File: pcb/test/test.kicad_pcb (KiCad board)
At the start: 2 copper layers, 12 parts, among them IC1 ADG904BRUZ-REEL7, J1 CONSMA013.062-G, J3 Conn_01x04, U1 MCP601R

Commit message: composants placés sur pcb
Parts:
- removed U1: MCP601R, Package_TO_SOT_SMD:SOT-23-5
- added ANT4: ST0147-00-011-A, test_footprint_library:ANTC3016X55N, F.Cu at (207.5, 20.0)
- added U2: TL081, Package_DIP:DIP-8_W7.62mm, F.Cu at (224.2, 135.7)
- moved C3 216.3 mm to (253.7, 131.5)
- moved R2 183.3 mm to (228.3, 114.0)
- moved R1 154.1 mm to (198.9, 111.0)
- moved C1 136.8 mm to (165.7, 150.5)
- moved C2 119.1 mm to (150.2, 149.5)
- moved ANT3 116.3 mm to (20.0, 20.0)
- moved ANT2 92.8 mm to (145.0, 20.0)
- moved ANT1 79.2 mm to (82.5, 20.0)
- moved J1 31.5 mm to (104.0, 168.6)
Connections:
- IC1 pad 14: unconnected-(IC1-RF4-Pad14) -> Net-(ANT4-FEED)

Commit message: pistes
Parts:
- added JP1: Jumper_2_Bridged, test_footprint_library:jumper20, F.Cu at (115.5, 96.5)
- added JP2: Jumper_2_Bridged, test_footprint_library:jumper20, F.Cu at (119.0, 91.0)
- moved C3 55.7 mm to (200.5, 115.0), turned to 90 degrees
- moved R2 41.8 mm to (187.5, 123.1), turned to 90 degrees
- moved R1 34.9 mm to (187.4, 144.0), turned to 90 degrees
- moved U2 21.2 mm to (205.4, 126.0), turned to -90 degrees
- moved C2 12.3 mm to (161.7, 145.0), turned to 180 degrees
- moved C1 5.80 mm to (161.5, 154.5), turned to 180 degrees
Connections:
- J3 pad 1: GND -> +5V
- J3 pad 2: Net-(IC1-A0) -> GND
- J3 pad 3: Net-(IC1-A1) -> Net-(J3-Pin_3)
- J3 pad 4: +5V -> Net-(J3-Pin_4)
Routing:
- net Net-(ANT4-FEED): track 0.00 -> 130.8 mm
- net +2V5: track 0.00 -> 129.6 mm
- net Net-(ANT3-FEED): track 0.00 -> 119.0 mm
- net GND: track 0.00 -> 99.2 mm
- net Net-(ANT2-FEED): track 0.00 -> 95.3 mm
- net Net-(ANT1-FEED): track 0.00 -> 88.7 mm
- net Net-(J3-Pin_4): track 0.00 -> 73.7 mm
- net Net-(J3-Pin_3): track 0.00 -> 69.8 mm
- net +5V: track 0.00 -> 67.9 mm
- net Net-(IC1-RFC): track 0.00 -> 63.6 mm
- net Net-(U2-+): track 0.00 -> 19.8 mm
- net Net-(IC1-A0): track 0.00 -> 11.3 mm
- net Net-(IC1-A1): track 0.00 -> 5.83 mm

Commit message: séance 18/12
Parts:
- moved J1 54.5 mm to (103.5, 114.1)
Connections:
- IC1 pad 12: unconnected-(IC1-GND_7-Pad12) -> GND
- IC1 pad 13: unconnected-(IC1-GND_8-Pad13) -> GND
- IC1 pad 15: unconnected-(IC1-GND_9-Pad15) -> GND
- IC1 pad 16: unconnected-(IC1-GND_10-Pad16) -> GND
- IC1 pad 18: unconnected-(IC1-GND_11-Pad18) -> GND
- IC1 pad 3: unconnected-(IC1-GND_1-Pad3) -> GND
- IC1 pad 5: unconnected-(IC1-GND_2-Pad5) -> GND
- IC1 pad 6: unconnected-(IC1-GND_3-Pad6) -> GND
- IC1 pad 8: unconnected-(IC1-GND_4-Pad8) -> GND
- IC1 pad 9: unconnected-(IC1-GND_5-Pad9) -> GND
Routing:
- net Net-(IC1-RFC): track 63.6 -> 0.00 mm
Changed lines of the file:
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@@
 	(net 9 "unconnected-(ANT3-NC-Pad2)")
 	(net 10 "Net-(IC1-A0)")
-	(net 11 "unconnected-(IC1-GND_7-Pad12)")
-	(net 12 "unconnected-(IC1-GND_4-Pad8)")
-	(net 13 "unconnected-(IC1-GND_9-Pad15)")
-	(net 14 "unconnected-(IC1-GND_8-Pad13)")
-	(net 15 "unconnected-(IC1-GND_3-Pad6)")
-	(net 16 "Net-(IC1-A1)")
-	(net 17 "unconnected-(IC1-GND_1-Pad3)")
-	(net 18 "unconnected-(IC1-GND_2-Pad5)")
-	(net 19 "unconnected-(IC1-GND_5-Pad9)")
-	(net 20 "unconnected-(IC1-GND_11-Pad18)")
-	(net 21 "Net-(IC1-RFC)")
-	(net 22 "unconnected-(IC1-GND_10-Pad16)")
-	(net 23 "Net-(U2-+)")
-	(net 24 "unconnected-(U2-NC-Pad8)")
-	(net 25 "unconnected-(U2-NULL-Pad1)")
-	(net 26 "unconnected-(U2-NULL-Pad5)")
-	(net 27 "unconnected-(ANT4-NC-Pad2)")
-	(net 28 "Net-(ANT4-FEED)")
-	(net 29 "Net-(J3-Pin_4)")
-	(net 30 "Net-(J3-Pin_3)")
+	(net 11 "Net-(IC1-A1)")
+	(net 12 "Net-(IC1-RFC)")
+	(net 13 "Net-(U2-+)")
+	(net 14 "unconnected-(U2-NC-Pad8)")
+	(net 15 "unconnected-(U2-NULL-Pad1)")
+	(net 16 "unconnected-(U2-NULL-Pad5)")
+	(net 17 "unconnected-(ANT4-NC-Pad2)")
+	(net 18 "Net-(ANT4-FEED)")
+	(net 19 "Net-(J3-Pin_4)")
+	(net 20 "Net-(J3-Pin_3)")
 	(footprint "Resistor_THT:R_Axial_DIN0411_L9.9mm_D3.6mm_P15.24mm_Horizontal"
 		(layer "F.Cu")
@@
 			(layers "*.Cu" "*.Mask")
 			(remove_unused_layers no)
-			(net 23 "Net-(U2-+)")
+			(net 13 "Net-(U2-+)")
 			(pintype "passive")
 		)
@@
 		(tags "capacitor electrolytic")
 		(property "Reference" "C2"
-			(at 0 -4.35 360)
+			(at 0 -4.35 0)
 			(layer "F.SilkS")
 			(effects
@@
 		)
 		(property "Value" "C_Polarized"
-			(at 0 4.35 360)
+			(at 0 4.35 0)
 			(layer "F.Fab")
 			(effects
@@
 		)
 		(fp_text user "${REFERENCE}"
-			(at 0 0 360)
+			(at 0 0 0)
 			(layer "F.Fab")
 			(effects
@@
 			(layers "*.Cu" "*.Mask")
 			(remove_unused_layers no)
-			(net 30 "Net-(J3-Pin_3)")
+			(net 20 "Net-(J3-Pin_3)")
 			(pinfunction "B")
 			(pintype "passive")
@@
 			(layers "*.Cu" "*.Mask")
 			(remove_unused_layers no)
-			(net 23 "Net-(U2-+)")
+			(net 13 "Net-(U2-+)")
 			(pintype "passive")
 		)
@@
 		(tags "capacitor electrolytic")
 		(property "Reference" "C1"
-			(at 0 -4.35 360)
+			(at 0 -4.35 0)
 			(layer "F.SilkS")
 			(effects
@@
 		)
 		(property "Value" "C"
-			(at 0 4.35 360)
+			(at 0 4.35 0)
 			(layer "F.Fab")
 			(effects
@@
 		)
 		(fp_text user "${REFERENCE}"
-			(at 0 0 360)
+			(at 0 0 0)
 			(layer "F.Fab")
 			(effects
@@
 			(layers "*.Cu" "*.Mask")
 			(remove_unused_layers no)
-			(net 16 "Net-(IC1-A1)")
+			(net 11 "Net-(IC1-A1)")
 			(pinfunction "A")
 			(pintype "passive")
@@
 			(layers "*.Cu" "*.Mask")
 			(remove_unused_layers no)
-			(net 29 "Net-(J3-Pin_4)")
+			(net 19 "Net-(J3-Pin_4)")
 			(pinfunction "B")
 			(pintype "passive")
@@
 			(size 0.45 1.475)
 			(layers "F.Cu" "F.Paste" "F.Mask")
-			(net 17 "unconnected-(IC1-GND_1-Pad3)")
+			(net 3 "GND")
 			(pinfunction "GND_1")
 			(pintype "passive")
@@
 			(size 0.45 1.475)
 			(layers "F.Cu" "F.Paste" "F.Mask")
-			(net 18 "unconnected-(IC1-GND_2-Pad5)")
+			(net 3 "GND")
 			(pinfunction "GND_2")
 			(pintype "passive")
@@
 			(size 0.45 1.475)
 			(layers "F.Cu" "F.Paste" "F.Mask")
-			(net 15 "unconnected-(IC1-GND_3-Pad6)")
+			(net 3 "GND")
 			(pinfunction "GND_3")
 			(pintype "passive")
@@
 			(size 0.45 1.475)
 			(layers "F.Cu" "F.Paste" "F.Mask")
-			(net 12 "unconnected-(IC1-GND_4-Pad8)")
+			(net 3 "GND")
 			(pinfunction "GND_4")
 			(pintype "passive")
@@
 			(size 0.45 1.475)
 			(layers "F.Cu" "F.Paste" "F.Mask")
-			(net 19 "unconnected-(IC1-GND_5-Pad9)")
+			(net 3 "GND")
 			(pinfunction "GND_5")
 			(pintype "passive")
@@
 			(size 0.45 1.475)
 			(layers "F.Cu" "F.Paste" "F.Mask")
-			(net 21 "Net-(IC1-RFC)")
+			(net 12 "Net-(IC1-RFC)")
 			(pinfunction "RFC")
 			(pintype "passive")
@@
 			(size 0.45 1.475)
 			(layers "F.Cu" "F.Paste" "F.Mask")
-			(net 11 "unconnected-(IC1-GND_7-Pad12)")
+			(net 3 "GND")
 			(pinfunction "GND_7")
 			(pintype "passive")
@@
 			(size 0.45 1.475)
 			(layers "F.Cu" "F.Paste" "F.Mask")
-			(net 14 "unconnected-(IC1-GND_8-Pad13)")
+			(net 3 "GND")
 			(pinfunction "GND_8")
 			(pintype "passive")
@@
 			(size 0.45 1.475)
 			(layers "F.Cu" "F.Paste" "F.Mask")
-			(net 28 "Net-(ANT4-FEED)")
+			(net 18 "Net-(ANT4-FEED)")
 			(pinfunction "RF4")
 			(pintype "passive")
@@
 			(size 0.45 1.475)
 			(layers "F.Cu" "F.Paste" "F.Mask")
-			(net 13 "unconnected-(IC1-GND_9-Pad15)")
+			(net 3 "GND")
 			(pinfunction "GND_9")
 			(pintype "passive")
@@
 			(size 0.45 1.475)
 			(layers "F.Cu" "F.Paste" "F.Mask")
-			(net 22 "unconnected-(IC1-GND_10-Pad16)")
+			(net 3 "GND")
 			(pinfunction "GND_10")
 			(pintype "passive")
@@
 			(size 0.45 1.475)
 			(layers "F.Cu" "F.Paste" "F.Mask")
-			(net 20 "unconnected-(IC1-GND_11-Pad18)")
+			(net 3 "GND")
 			(pinfunction "GND_11")
 			(pintype "passive")
@@
 			(size 0.45 1.475)
 			(layers "F.Cu" "F.Paste" "F.Mask")
-			(net 16 "Net-(IC1-A1)")
+			(net 11 "Net-(IC1-A1)")
 			(pinfunction "A1")
 			(pintype "passive")
@@
 	(footprint "test_footprint_library:LINX_CONSMA013.062-G"
 		(layer "F.Cu")
-		(at 104 168.6375)
+		(at 103.5 114.1375)
 		(property "Reference" "J1"
 			(at -2.978 -6.9964 0)
@@
 			(size 1.52 5.08)
 			(layers "F.Cu" "F.Paste" "F.Mask")
-			(net 21 "Net-(IC1-RFC)")
+			(net 12 "Net-(IC1-RFC)")
 			(pintype "passive")
 			(solder_mask_margin 0.102)
@@
 			(layers "*.Cu" "*.Mask")
 			(remove_unused_layers no)
-			(net 25 "unconnected-(U2-NULL-Pad1)")
+			(net 15 "unconnected-(U2-NULL-Pad1)")
 			(pinfunction "NULL")
 			(pintype "input")
@@
 			(layers "*.Cu" "*.Mask")
 			(remove_unused_layers no)
-			(net 23 "Net-(U2-+)")
+			(net 13 "Net-(U2-+)")
 			(pinfunction "+")
 			(pintype "input")
@@
 			(layers "*.Cu" "*.Mask")
 			(remove_unused_layers no)
-			(net 26 "unconnected-(U2-NULL-Pad5)")
+			(net 16 "unconnected-(U2-NULL-Pad5)")
 			(pinfunction "NULL")
 			(pintype "input")
@@
 			(layers "*.Cu" "*.Mask")
 			(remove_unused_layers no)
-			(net 24 "unconnected-(U2-NC-Pad8)")
+			(net 14 "unconnected-(U2-NC-Pad8)")
 			(pinfunction "NC")
 			(pintype "no_connect")
@@
 			(size 0.8 1.75)
 			(layers "F.Cu" "F.Paste" "F.Mask")
-			(net 28 "Net-(ANT4-FEED)")
+			(net 18 "Net-(ANT4-FEED)")
 			(pinfunction "FEED")
 			(pintype "input")
@@
 			(size 0.8 1.75)
 			(layers "F.Cu" "F.Paste" "F.Mask")
-			(net 27 "unconnected-(ANT4-NC-Pad2)")
+			(net 17 "unconnected-(ANT4-NC-Pad2)")
 			(pinfunction "NC")
 			(pintype "no_connect")
@@
 			(layers "*.Cu" "*.Mask")
 			(remove_unused_layers no)
-			(net 30 "Net-(J3-Pin_3)")
+			(net 20 "Net-(J3-Pin_3)")
 			(pinfunction "Pin_3")
 			(pintype "passive")
@@
 			(layers "*.Cu" "*.Mask")
 			(remove_unused_layers no)
-			(net 29 "Net-(J3-Pin_4)")
+			(net 19 "Net-(J3-Pin_4)")
 			(pinfunction "Pin_4")
 			(pintype "passive")
@@
 		(width 0.2)
 		(layer "F.Cu")
-		(net 16)
+		(net 11)
 	)
 	(segment
@@
 		(width 0.2)
 		(layer "F.Cu")
-		(net 16)
-	)
-	(segment
-		(start 104 164.3175)
-		(end 104.124 164.1935)
-		(width 0.2)
-		(layer "F.Cu")
-		(net 21)
-	)
-	(segment
-		(start 104.124 164.1935)
-		(end 104.124 102.5)
-		(width 0.2)
-		(layer "F.Cu")
-		(net 21)
-	)
-	(segment
-		(start 104 166.0975)
-		(end 104 164.3175)
-		(width 0.2)
-		(layer "F.Cu")
-		(net 21)
+		(net 11)
 	)
 	(segment
@@
 		(width 0.2)
 		(layer "F.Cu")
-		(net 23)
+		(net 13)
 	)
 	(segment
@@
 		(width 0.2)
 		(layer "F.Cu")
-		(net 23)
+		(net 13)
 	)
 	(segment
@@
 		(width 0.2)
 		(layer "F.Cu")
-		(net 23)
+		(net 13)
 	)
 	(segment
@@
 		(width 0.2)
 		(layer "F.Cu")
-		(net 23)
+		(net 13)
 	)
 	(segment
@@
 		(width 0.2)
 		(layer "F.Cu")
-		(net 28)
+		(net 18)
 	)
 	(segment
@@
 		(width 0.2)
 		(layer "F.Cu")
-		(net 28)
+		(net 18)
 	)
 	(segment
@@
 		(width 0.2)
 		(layer "F.Cu")
-		(net 28)
+		(net 18)
 	)
 	(segment
@@
 		(width 0.2)
 		(layer "F.Cu")
-		(net 28)
+		(net 18)
 	)
 	(segment
@@
 		(width 0.2)
 		(layer "F.Cu")
-		(net 29)
+		(net 19)
 	)
 	(segment
@@
 		(width 0.2)
 		(layer "F.Cu")
-		(net 29)
+		(net 19)
 	)
 	(segment
@@
 		(width 0.2)
 		(layer "F.Cu")
-		(net 29)
+		(net 19)
 	)
 	(segment
@@
 		(width 0.2)
 		(layer "F.Cu")
-		(net 30)
+		(net 20)
 	)
 	(segment
@@
 		(width 0.2)
 		(layer "F.Cu")
-		(net 30)
+		(net 20)
 	)
 )

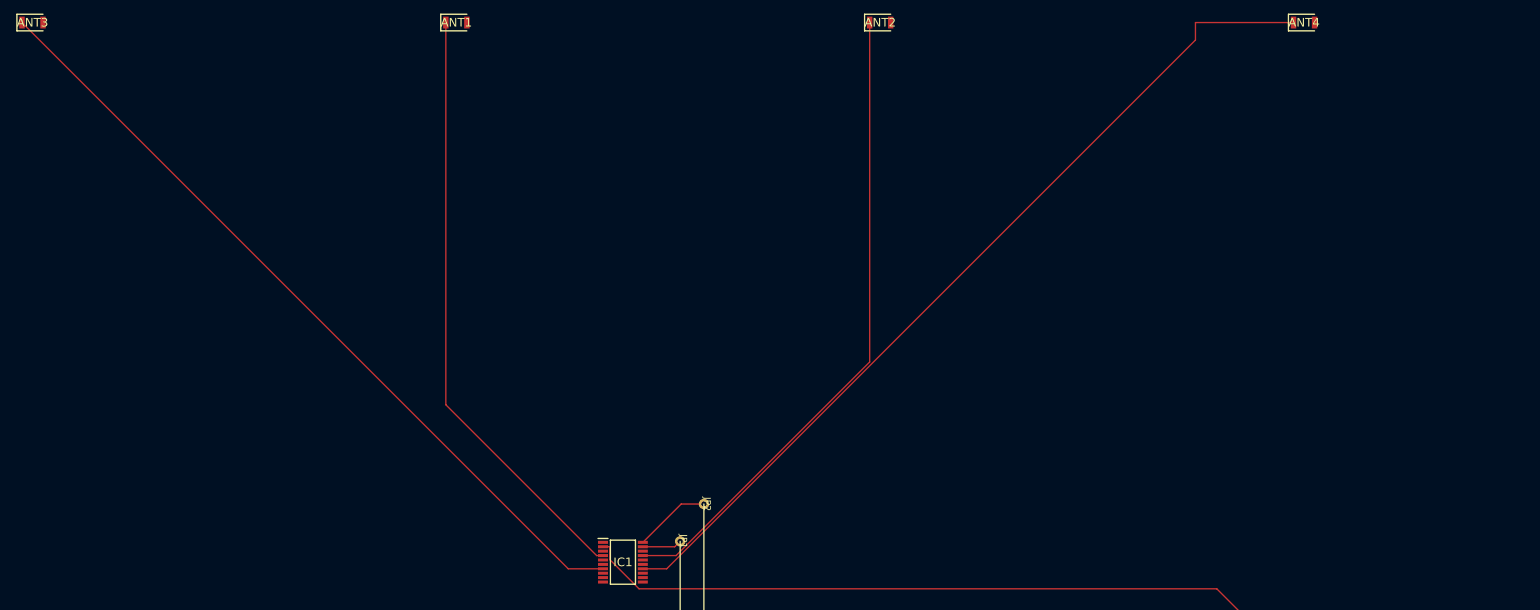
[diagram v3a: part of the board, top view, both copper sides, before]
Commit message: circuit adaptation impédance
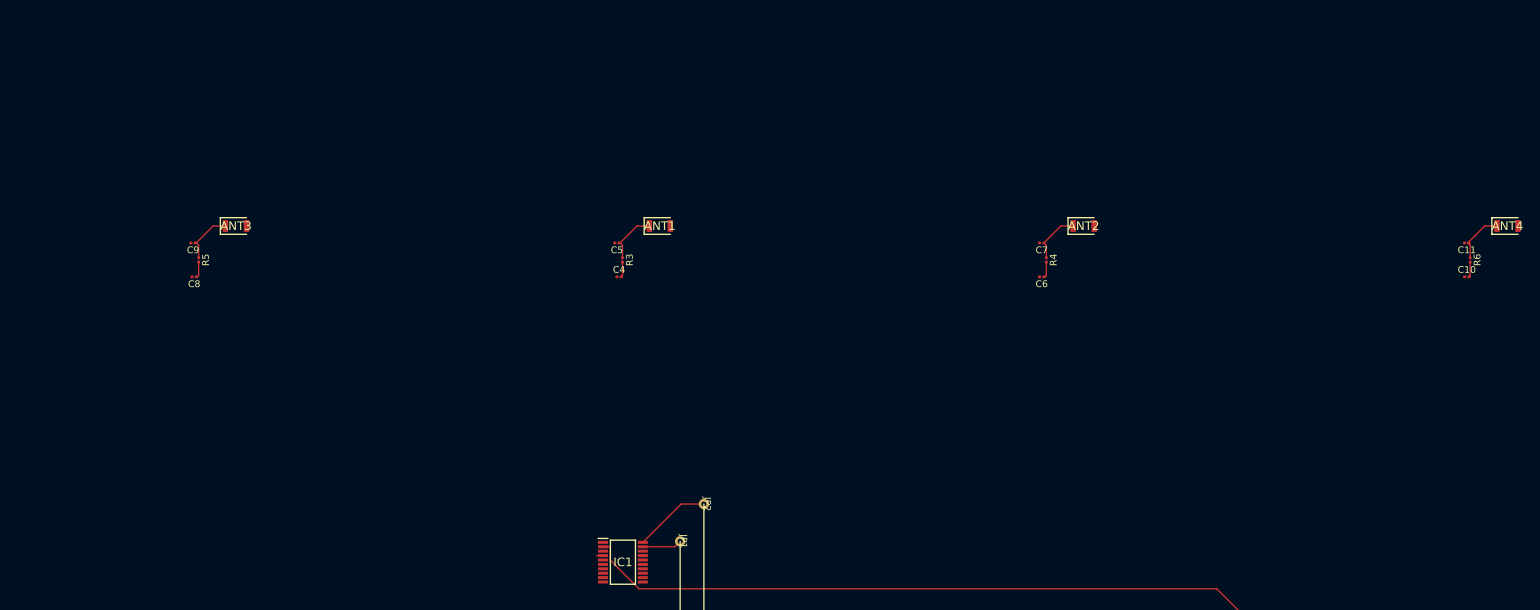
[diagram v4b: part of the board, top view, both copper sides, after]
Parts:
- added C10: C, Capacitor_SMD:C_0201_0603Metric, F.Cu at (231.5, 57.5)
- added C11: C, Capacitor_SMD:C_0201_0603Metric, F.Cu at (231.5, 52.5)
- added C4: C, Capacitor_SMD:C_0201_0603Metric, F.Cu at (106.5, 57.5)
- added C5: C, Capacitor_SMD:C_0201_0603Metric, F.Cu at (106.2, 52.5)
- added C6: C, Capacitor_SMD:C_0201_0603Metric, F.Cu at (168.8, 57.5)
- added C7: C, Capacitor_SMD:C_0201_0603Metric, F.Cu at (168.8, 52.5)
- added C8: C, Capacitor_SMD:C_0201_0603Metric, F.Cu at (43.8, 57.5)
- added C9: C, Capacitor_SMD:C_0201_0603Metric, F.Cu at (43.7, 52.5)
- added R3: 0, Resistor_SMD:R_0201_0603Metric, F.Cu at (107.0, 55.0)
- added R4: 0, Resistor_SMD:R_0201_0603Metric, F.Cu at (169.5, 55.0)
- added R5: 0, Resistor_SMD:R_0201_0603Metric, F.Cu at (44.5, 55.0)
- added R6: 0, Resistor_SMD:R_0201_0603Metric, F.Cu at (232.0, 55.0)
- moved ANT1 42.4 mm to (112.5, 50.0)
- moved ANT2 42.4 mm to (175.0, 50.0)
- moved ANT3 42.4 mm to (50.0, 50.0)
- moved ANT4 42.4 mm to (237.5, 50.0)
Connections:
- IC1 pad 14: Net-(ANT4-FEED) -> Net-(IC1-RF4)
- IC1 pad 17: Net-(ANT2-FEED) -> Net-(IC1-RF2)
- IC1 pad 4: Net-(ANT1-FEED) -> Net-(IC1-RF1)
- IC1 pad 7: Net-(ANT3-FEED) -> Net-(IC1-RF3)
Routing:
- net Net-(ANT4-FEED): track 130.8 -> 7.67 mm
- net Net-(ANT3-FEED): track 119.0 -> 7.67 mm
- net Net-(ANT2-FEED): track 95.3 -> 7.67 mm
- net Net-(ANT1-FEED): track 88.7 -> 7.67 mm
- net Net-(IC1-RF1): track 0.00 -> 3.19 mm
- net Net-(IC1-RF4): track 0.00 -> 2.25 mm
- net Net-(IC1-RF2): track 0.00 -> 2.25 mm
- net Net-(IC1-RF3): track 0.00 -> 2.25 mm

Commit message: je commence à comprendre comment les zones fonctionnent
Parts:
- moved JP2 61.2 mm to (162.0, 134.5)
- moved U2 59.2 mm to (258.2, 152.6)
- moved C1 59.2 mm to (214.3, 181.1)
- moved C2 59.2 mm to (214.5, 171.6)
- moved C3 59.2 mm to (253.3, 141.6)
- moved R1 59.2 mm to (240.2, 170.6)
- moved R2 59.2 mm to (240.3, 149.7)
- moved JP1 51.2 mm to (134.5, 144.0)
- moved IC1 42.9 mm to (150.0, 100.0)
- moved J1 32.6 mm to (135.5, 120.6)
- moved J3 32.6 mm to (193.0, 171.9)
- moved R5 10.4 mm to (34.5, 58.0)
- moved C9 9.37 mm to (34.3, 53.0)
- moved C8 9.32 mm to (36.3, 63.0)
- moved C6 1.86 mm to (170.7, 57.5)
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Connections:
- ANT1 pad 2: unconnected-(ANT1-NC-Pad2) -> GND
- ANT2 pad 2: unconnected-(ANT2-NC-Pad2) -> GND
- ANT3 pad 2: unconnected-(ANT3-NC-Pad2) -> GND
- ANT4 pad 2: unconnected-(ANT4-NC-Pad2) -> GND
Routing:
- net +2V5: track 129.6 -> 35.5 mm
- net Net-(J3-Pin_4): track 73.7 -> 0.00 mm
- net Net-(J3-Pin_3): track 69.8 -> 0.00 mm
- net +5V: track 67.9 -> 45.9 mm
- net GND: track 99.2 -> 78.8 mm
- net Net-(IC1-A0): track 11.3 -> 0.00 mm
- net Net-(ANT4-FEED): track 7.67 -> 0.00 mm
- net Net-(ANT2-FEED): track 7.67 -> 0.00 mm
- net Net-(ANT3-FEED): track 7.67 -> 0.00 mm
- net Net-(ANT1-FEED): track 7.67 -> 0.00 mm
- net Net-(IC1-A1): track 5.83 -> 0.00 mm
- net Net-(IC1-RF1): track 3.19 -> 0.00 mm
- net Net-(IC1-RF4): track 2.25 -> 0.00 mm
- net Net-(IC1-RF2): track 2.25 -> 0.00 mm
- net Net-(IC1-RF3): track 2.25 -> 0.00 mm
- added copper zone on F.Cu, net GND
